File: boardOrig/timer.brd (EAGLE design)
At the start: 99.4 x 44.6 mm, 46 parts, among them IC1 7805T, IC6 DS1307, U1 ATMEGA328P

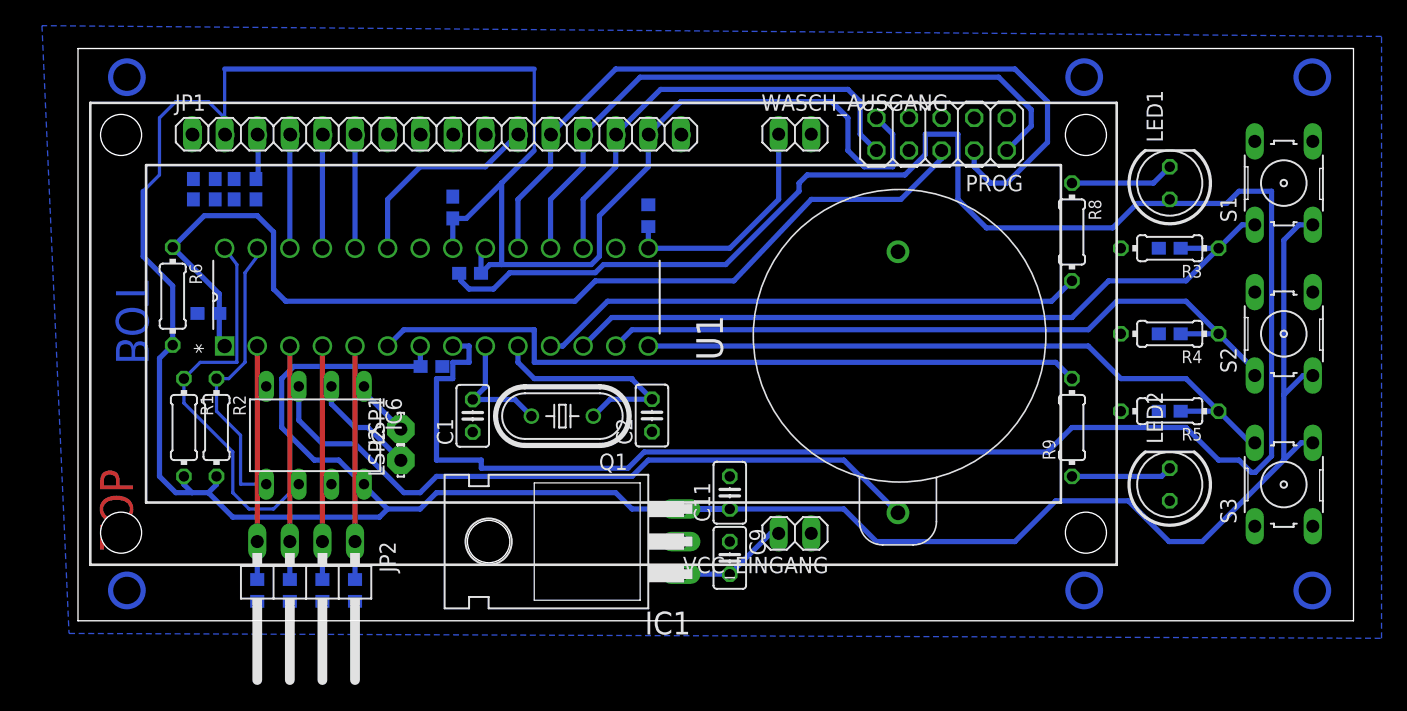
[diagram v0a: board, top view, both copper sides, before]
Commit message: Updated Board and added DS1307 to Program
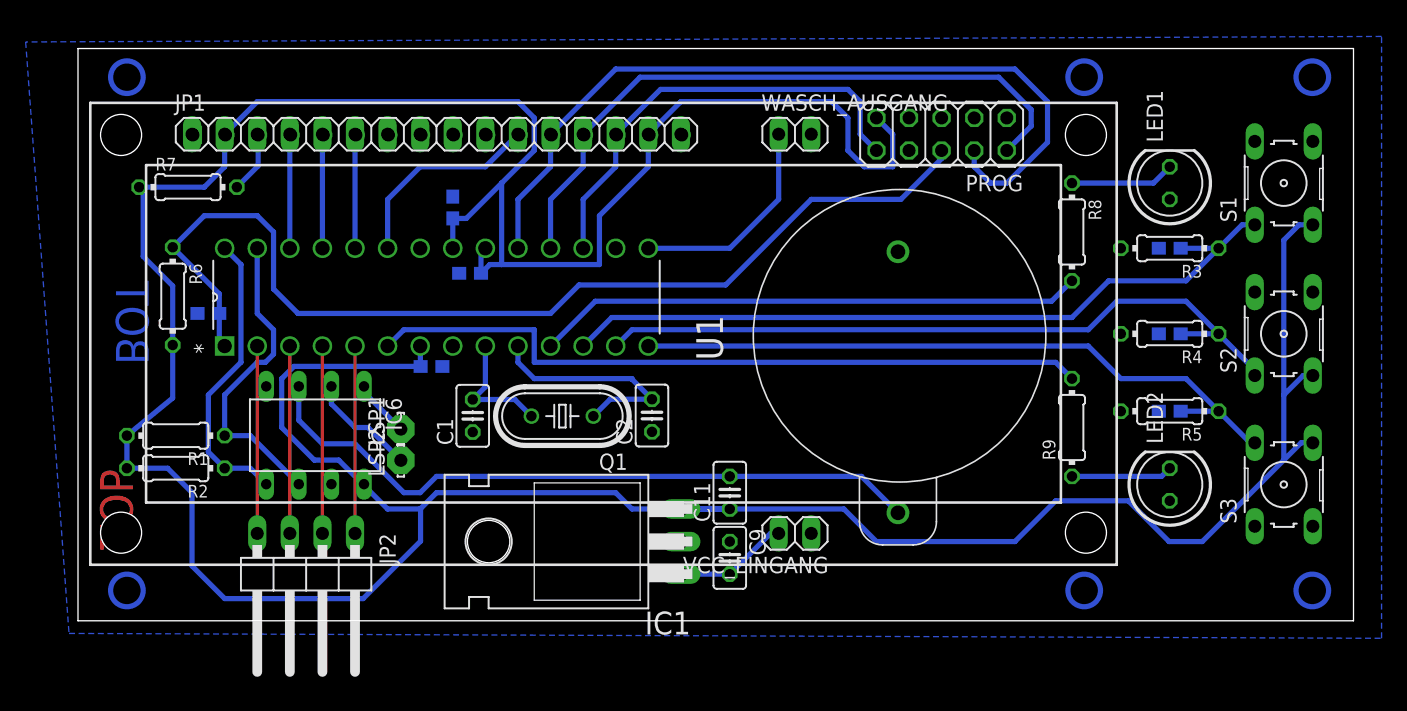
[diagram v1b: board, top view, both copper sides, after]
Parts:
- removed R10, R11, R12, R13, R14, R15, R16, R17: (no value), eagle-ltspice:R0603
- R7: value (none) -> 10k; device eagle-ltspice:R0603 -> resistor:0204/7
- moved R7 35.9 mm to (9.84, 34.0), flipped to the top, turned to 0 degrees
- moved R2 4.49 mm to (8.89, 12.1), turned to 180 degrees
- moved R1 0.90 mm to (8.89, 14.6), turned to 180 degrees
- moved JP2 0.63 mm to (19.1, 3.17)
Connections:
- removed net N$15: JP2.4, R14.2, U1.2
- removed net N$17: JP2.2, R16.2, U1.4
- new net N$10: JP2.2, U1.4
- new net N$6: JP2.4, U1.2
- net GND: no longer R10.1, R14.1, R15.1, R16.1, R17.1, R7.2
- net N$12: no longer R17.2
- net N$2: now also R7.2; no longer R13.2
- net N$3: no longer R7.1
- net N$39: now also U1.27; no longer U1.28
- net N$40: now also U1.28; no longer U1.27
- net N$9: no longer R15.2
- net VCC: now also R7.1
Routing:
- net GND: track 179.9 -> 0.00 mm
- net N$17: track 18.2 -> 0.00 mm
- net N$15: track 18.2 -> 0.00 mm
- net N$6: track 0.00 -> 14.6 mm
- net N$10: track 0.00 -> 14.6 mm
- net N$39: track 30.8 -> 24.4 mm
- net N$9: track 18.2 -> 14.6 mm
- net N$12: track 18.2 -> 14.6 mm
- net VCC: track 297.8 -> 300.6 mm
- net N$3: track 18.5 -> 16.8 mm
- net N$2: track 3.70 -> 4.85 mm
- net N$38: track 54.4 -> 53.4 mm
- net N$5: track 81.0 -> 81.7 mm
